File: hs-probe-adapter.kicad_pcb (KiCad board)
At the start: 2 copper layers, 20 x 16 mm, 5 parts, among them J1 STDC14, J2 ARM SWD, J3 UART, J4 SWD, J5 BluePill

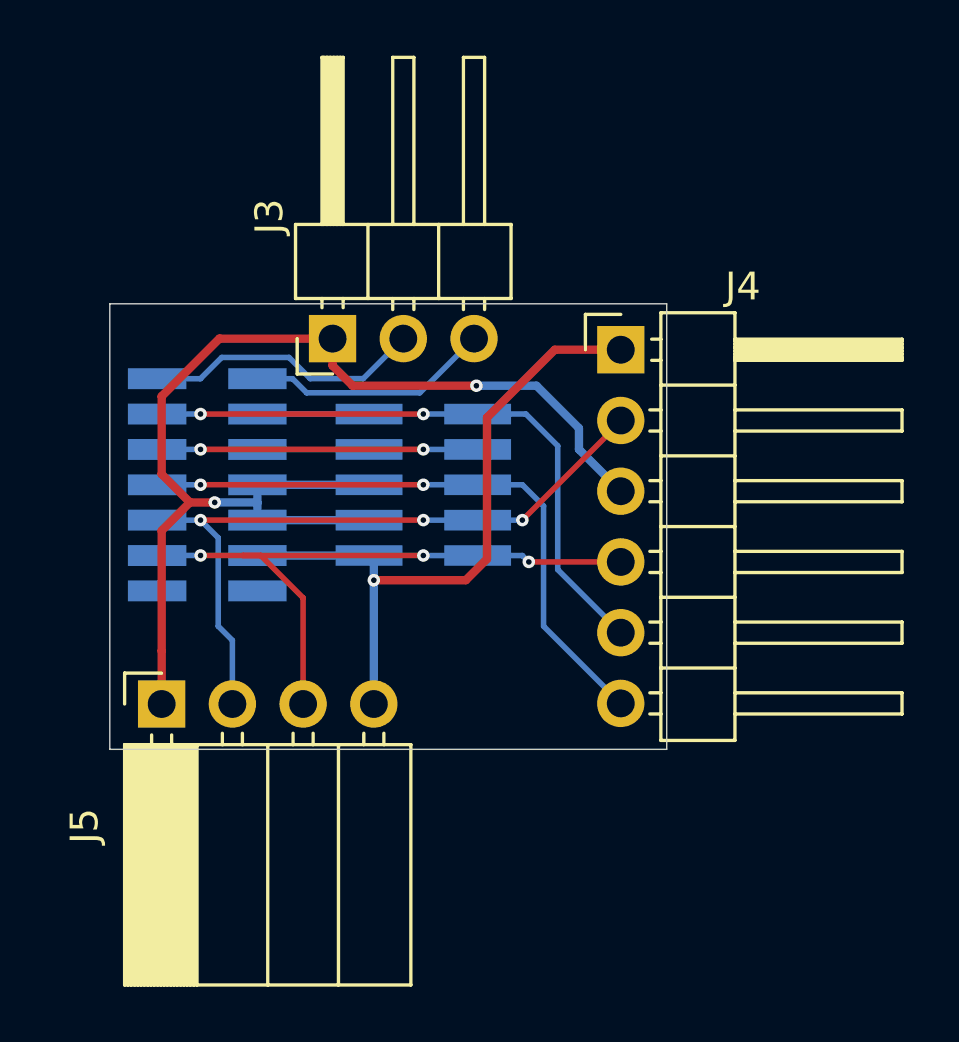
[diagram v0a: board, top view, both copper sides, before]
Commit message: Convert to KiCad 6.0
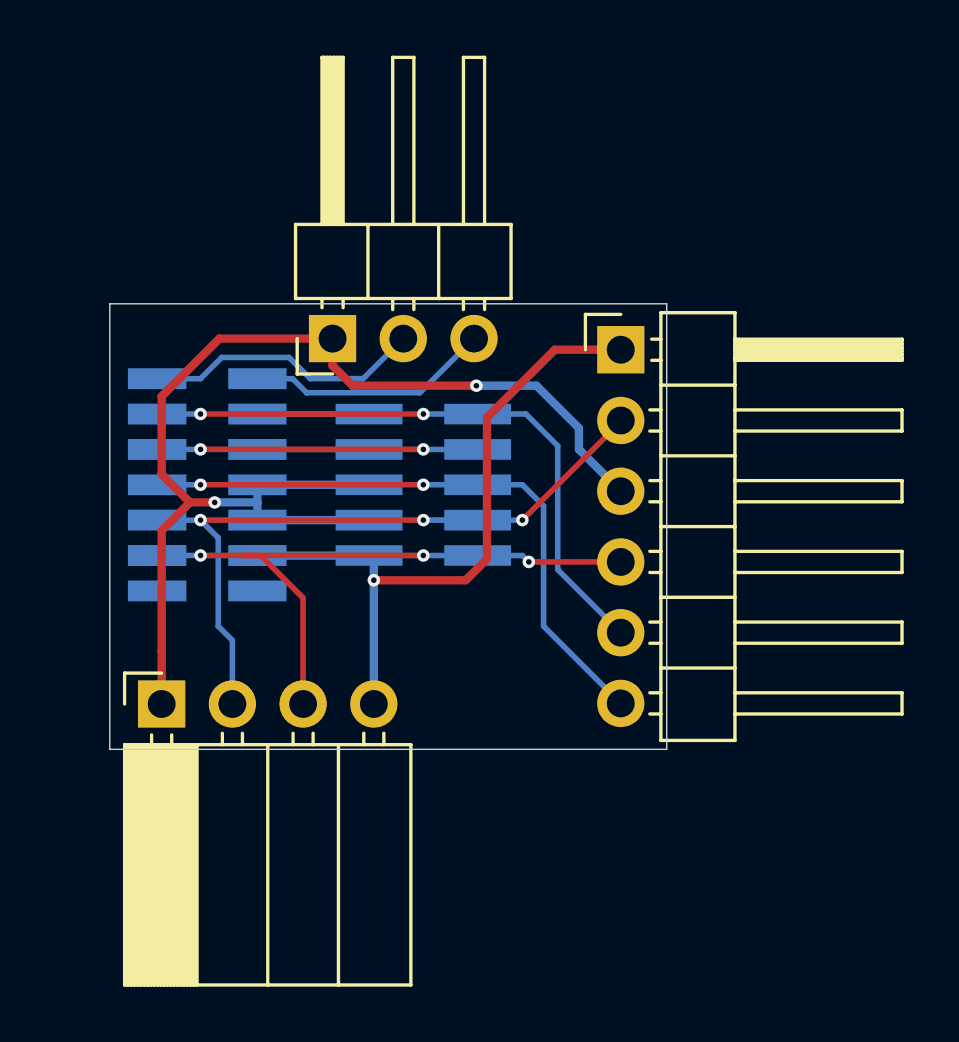
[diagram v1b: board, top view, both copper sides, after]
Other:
- net class Default removed
- net class Power removed

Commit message: Add silkscreen
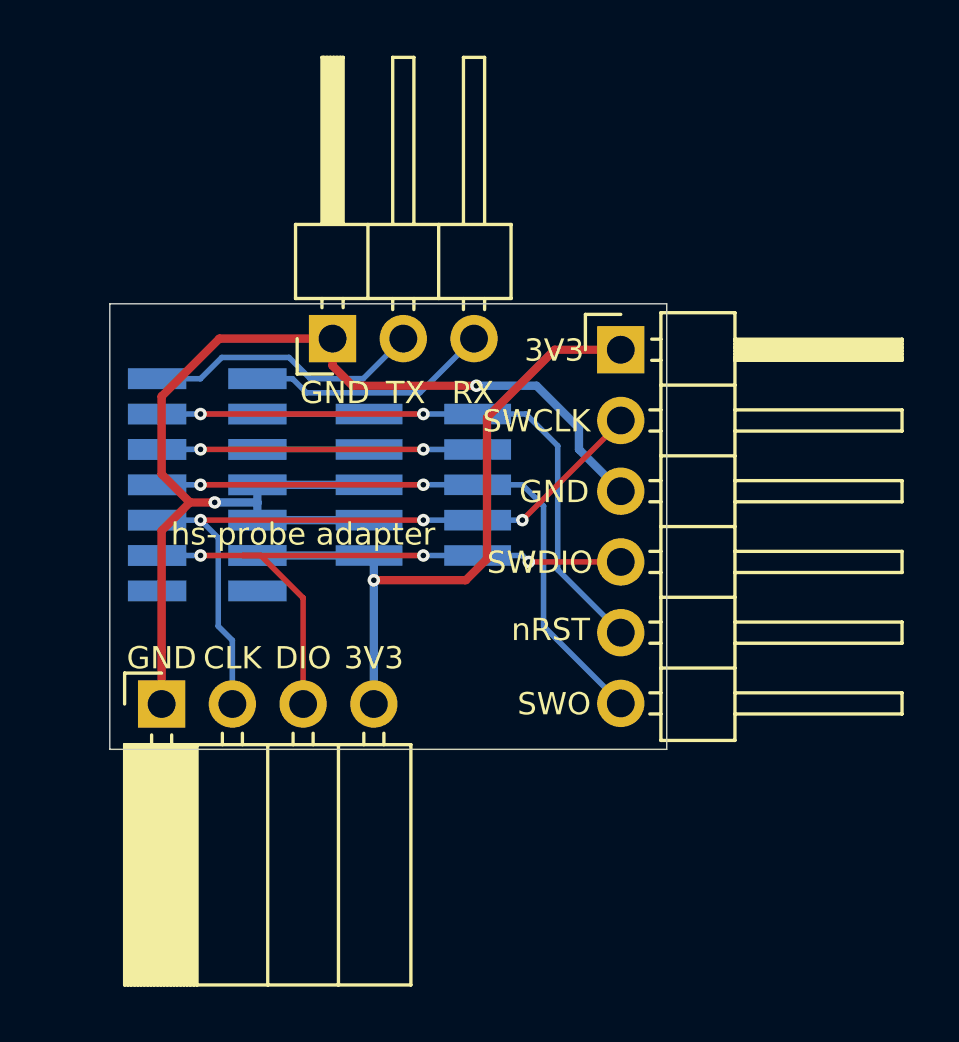
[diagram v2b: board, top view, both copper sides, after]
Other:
- board text added: "."
- board text added: "3V3"
- board text added: "CLK"
- board text added: "DIO"
- board text added: "GND"
- board text added: "JLCJLCJLCJLC"
- board text added: "RX"
- board text added: "SWCLK"
- board text added: "SWDIO"
- board text added: "SWO"
- board text added: "TX"
- board text added: "hs-probe adapter"
- board text added: "nRST"
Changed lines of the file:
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@@
   (gr_line (start 37 41) (end 57 41) (layer "Edge.Cuts") (width 0.05))
   (gr_line (start 57 57) (end 37 57) (layer "Edge.Cuts") (width 0.05))
+  (gr_text "." (at 45.466 50.673) (layer "B.SilkS")
+    (effects (font (size 0.8 0.8) (thickness 0.15)))
+  )
+  (gr_text "." (at 43.053 51.943) (layer "B.SilkS")
+    (effects (font (size 0.8 0.8) (thickness 0.15)))
+  )
+  (gr_text "JLCJLCJLCJLC" (at 44.323 47.752 -90) (layer "B.SilkS")
+    (effects (font (size 0.8 0.8) (thickness 0.15)) (justify mirror))
+  )
+  (gr_text "SWDIO" (at 52.451 50.292) (layer "F.SilkS")
+    (effects (font (size 0.8 0.8) (thickness 0.15)))
+  )
+  (gr_text "GND" (at 38.862 53.721) (layer "F.SilkS")
+    (effects (font (size 0.8 0.8) (thickness 0.15)))
+  )
+  (gr_text "CLK" (at 41.402 53.721) (layer "F.SilkS")
+    (effects (font (size 0.8 0.8) (thickness 0.15)))
+  )
+  (gr_text "hs-probe adapter" (at 43.942 49.276) (layer "F.SilkS")
+    (effects (font (size 0.8 0.8) (thickness 0.15)))
+  )
+  (gr_text "GND" (at 52.959 47.752) (layer "F.SilkS")
+    (effects (font (size 0.8 0.8) (thickness 0.15)))
+  )
+  (gr_text "GND" (at 45.085 44.196) (layer "F.SilkS")
+    (effects (font (size 0.8 0.8) (thickness 0.15)))
+  )
+  (gr_text "RX" (at 50.038 44.196) (layer "F.SilkS")
+    (effects (font (size 0.8 0.8) (thickness 0.15)))
+  )
+  (gr_text "SWCLK" (at 52.324 45.212) (layer "F.SilkS")
+    (effects (font (size 0.8 0.8) (thickness 0.15)))
+  )
+  (gr_text "nRST" (at 52.832 52.705) (layer "F.SilkS")
+    (effects (font (size 0.8 0.8) (thickness 0.15)))
+  )
+  (gr_text "DIO" (at 43.942 53.721) (layer "F.SilkS")
+    (effects (font (size 0.8 0.8) (thickness 0.15)))
+  )
+  (gr_text "3V3" (at 52.959 42.672) (layer "F.SilkS")
+    (effects (font (size 0.8 0.8) (thickness 0.15)))
+  )
+  (gr_text "SWO" (at 52.959 55.372) (layer "F.SilkS")
+    (effects (font (size 0.8 0.8) (thickness 0.15)))
+  )
+  (gr_text "3V3" (at 46.482 53.721) (layer "F.SilkS")
+    (effects (font (size 0.8 0.8) (thickness 0.15)))
+  )
+  (gr_text "TX" (at 47.625 44.196) (layer "F.SilkS")
+    (effects (font (size 0.8 0.8) (thickness 0.15)))
+  )
   (segment (start 43.435998 42.926) (end 44.197998 43.688) (width 0.2) (layer "B.Cu") (net 1))
   (segment (start 44.197998 43.688) (end 46.102 43.688) (width 0.2) (layer "B.Cu") (net 1))
